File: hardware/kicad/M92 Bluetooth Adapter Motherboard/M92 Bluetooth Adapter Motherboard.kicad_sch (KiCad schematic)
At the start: 26 parts, among them IC1 PIC18F27Q43-I/SO, J2 Conn_Handset_RJ45, J6 Conn_MCU_Programming, J7 Conn_BT_Module, J8 Conn_MCU_IO_UART, Q2 PN2222ATA

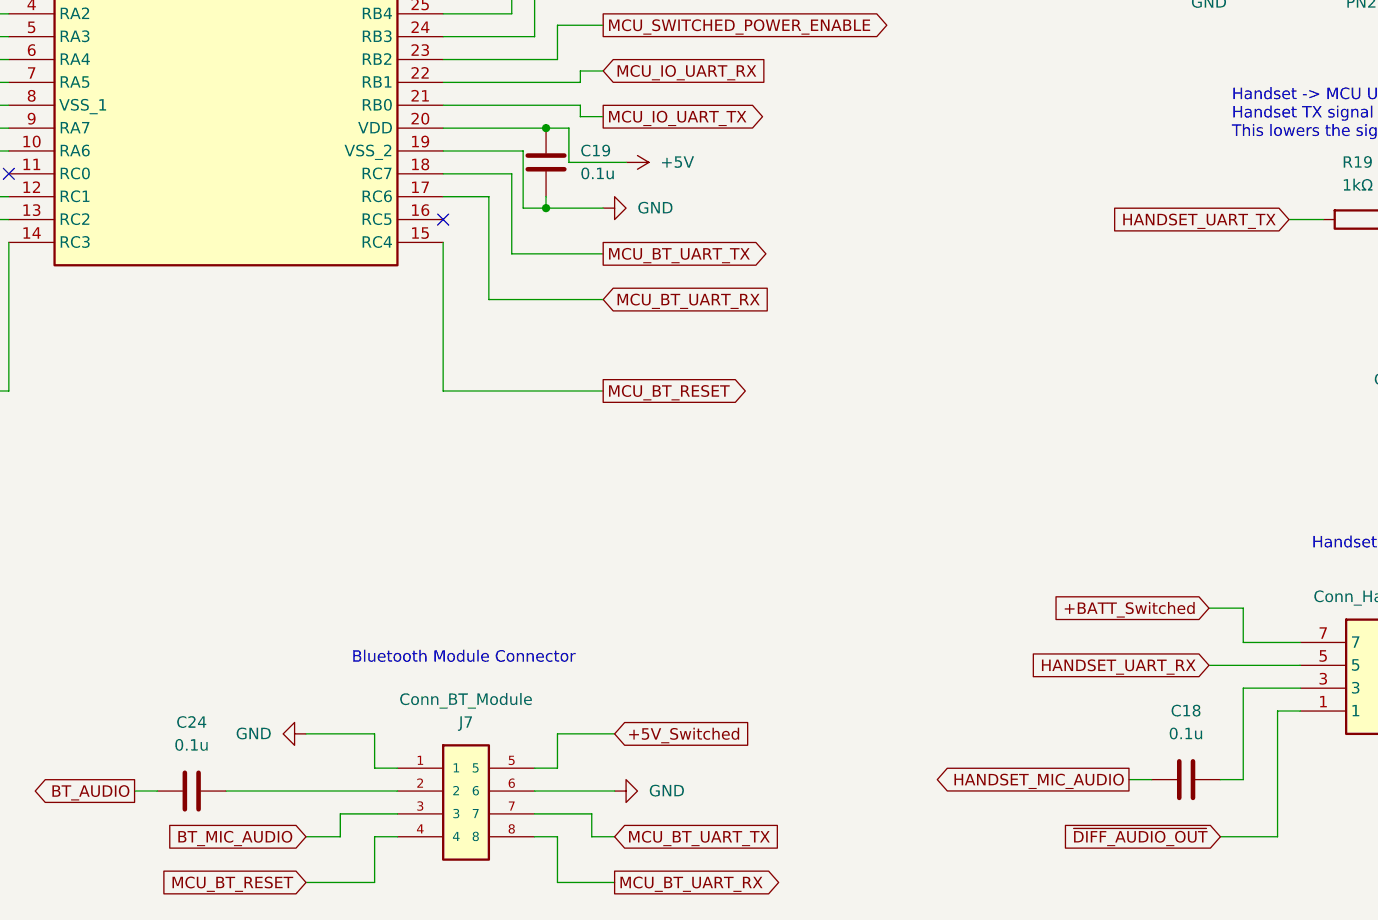
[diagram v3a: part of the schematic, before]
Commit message: Motherboard circuit/PCB adjustments
* Add 100uf cap to stabilize the 5V power supply (reduce voltage dip during power-on of switched 5V supply).
* Add cap to 12V load switch to reduce inrush current when powering on handset.
* Part number updates to more readily available parts.
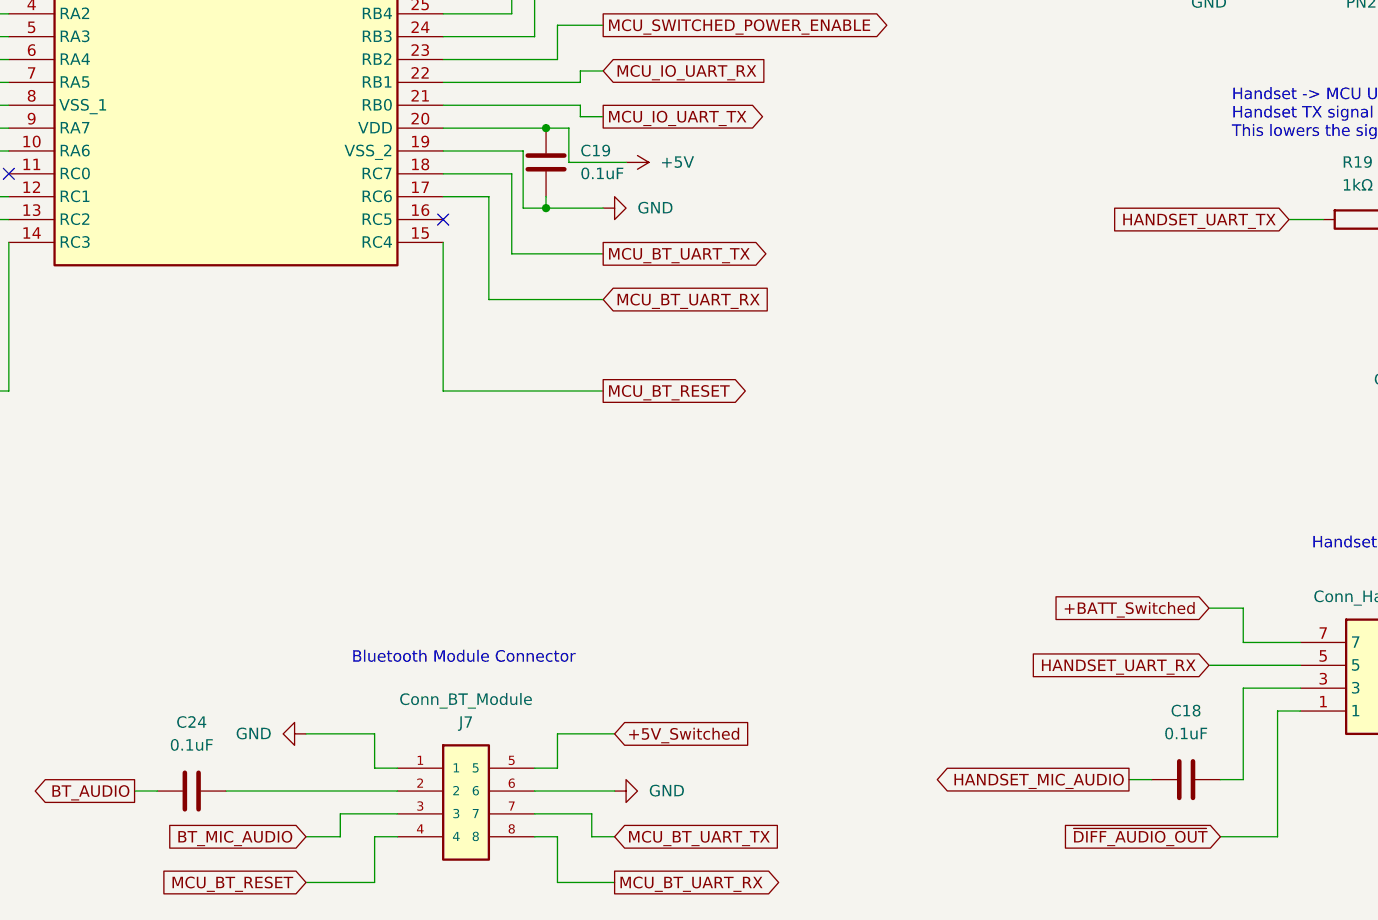
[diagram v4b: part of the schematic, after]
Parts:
- C18, C19, C24: value 0.1u -> 0.1uF
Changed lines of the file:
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@@
       (effects (font (size 1.27 1.27)))
     )
-    (property "Value" "0.1u" (at 96.52 143.51 90)
+    (property "Value" "0.1uF" (at 96.52 143.51 90)
       (effects (font (size 1.27 1.27)))
     )
@@
       (effects (font (size 1.27 1.27)) (justify right))
     )
-    (property "Value" "0.1u" (at 139.7 80.01 0)
+    (property "Value" "0.1uF" (at 139.7 80.01 0)
       (effects (font (size 1.27 1.27)) (justify right))
     )
@@
       (effects (font (size 1.27 1.27)))
     )
-    (property "Value" "0.1u" (at 207.01 142.24 90)
-      (effects (font (size 1.27 1.27)))
-    )
+    (property "Value" "0.1uF" (at 207.01 142.24 90)
+      (effects (font (size 1.27 1.27)))
+    )

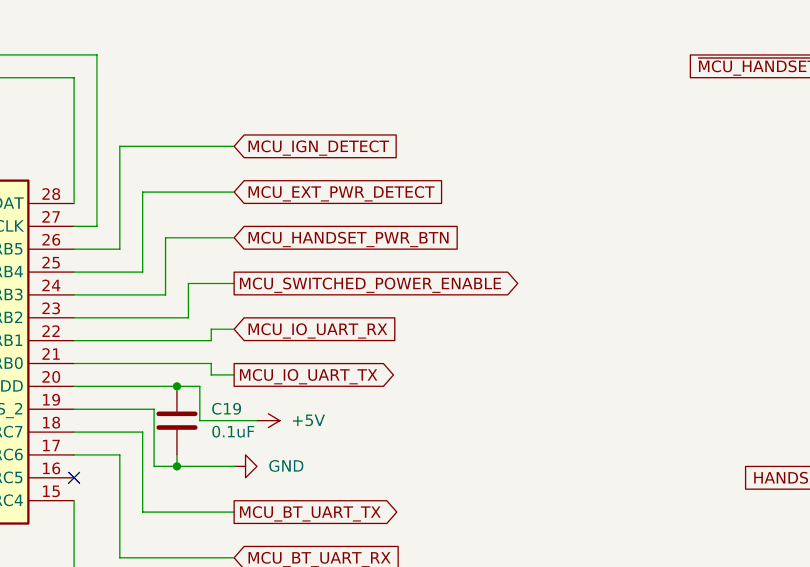
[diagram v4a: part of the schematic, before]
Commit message: Keep handset powered on during restarts
Inverted the switched power enable signal from the MCU with a transistor so that switched power is on by default unless the MCU explicitly disables it. This allows everything to remain powered on while the MCU reboots for a restart. If the MCU is rebooting to power off, then it immediately turns switched power off before entering the sleep state.

This is simpler and more robust than attempting to write code to fully reinitialize ALL MCU state/memory except for switched power enable output.
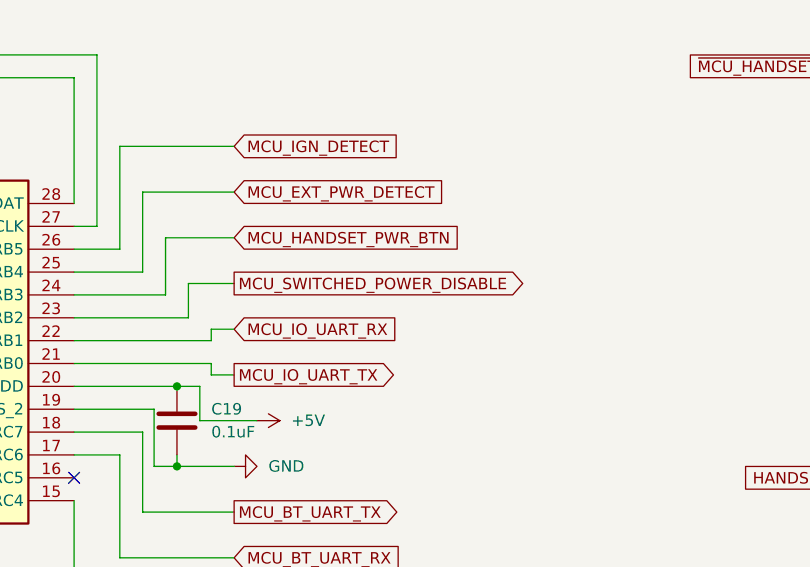
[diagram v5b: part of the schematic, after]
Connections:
- net MCU_SWITCHED_POWER_ENABLE renamed MCU_SWITCHED_POWER_DISABLE
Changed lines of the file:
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@@
     )
   )
-  (global_label "MCU_SWITCHED_POWER_ENABLE" (shape output) (at 142.24 63.5 0) (fields_autoplaced)
+  (global_label "MCU_SWITCHED_POWER_DISABLE" (shape output) (at 142.24 63.5 0) (fields_autoplaced)
     (effects (font (size 1.27 1.27)) (justify left))
-    (property "Intersheetrefs" "${INTERSHEET_REFS}" (at 174.9188 63.5 0)
+    (property "Intersheetrefs" "${INTERSHEET_REFS}" (at 175.5236 63.5 0)
       (effects (font (size 1.27 1.27)) (justify left))
     )

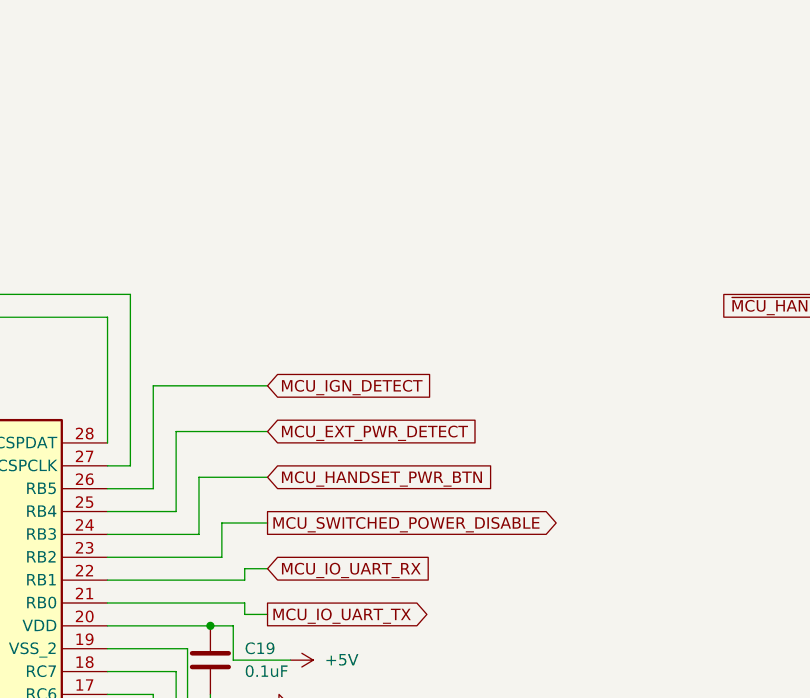
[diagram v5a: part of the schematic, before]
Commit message: Simplify load switch enable circuit, and add 100uF cap to 12V supply
Eliminated the load switch enable inverting transistor and simplified to a combination of a pull-up resistor on the enable pin with open-drain and initially high configuration of the MCU pin.

This still keeps the load switches enabled during a MCU reboot like the previous design, but with fewer components and less wasted power.

Also added a 100uF capacitor to the 12V supply to help reduce voltage dips.
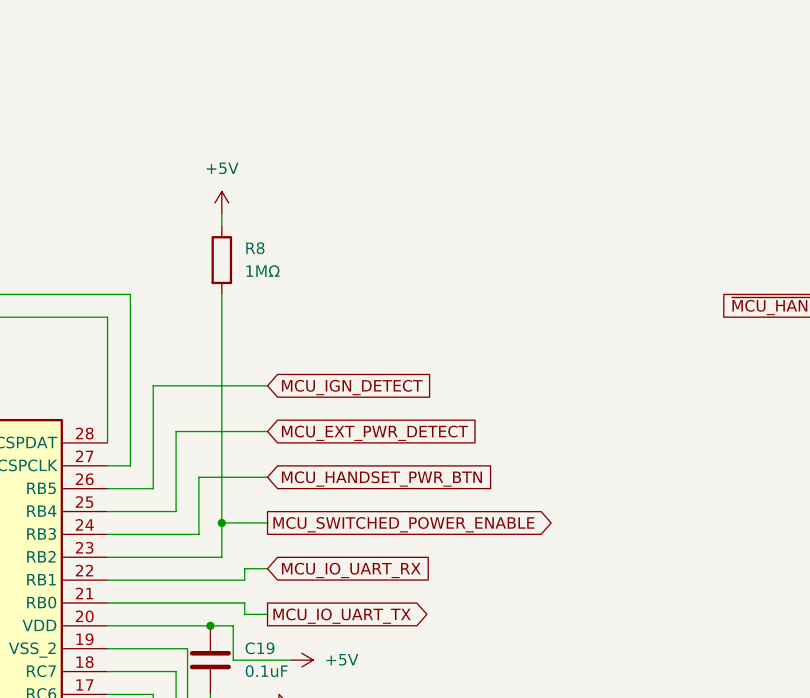
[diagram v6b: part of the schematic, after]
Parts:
- added R8: 1MΩ, Resistor_SMD:R_1206_3216Metric_Pad1.30x1.75mm_HandSolder, symbol Device:R
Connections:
- net +5V: now also R8.1
- net MCU_SWITCHED_POWER_DISABLE renamed MCU_SWITCHED_POWER_ENABLE
- net MCU_SWITCHED_POWER_ENABLE: now also R8.2
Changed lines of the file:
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@@
   (junction (at 135.89 83.82) (diameter 0) (color 0 0 0 0)
+  )
+  (junction (at 137.16 63.5) (diameter 0) (color 0 0 0 0)
   )
   (junction (at 76.2 39.37) (diameter 0) (color 0 0 0 0)
@@
     (stroke (width 0) (type default))
   )
+  (wire (pts (xy 137.16 38.1) (xy 137.16 63.5))
+    (stroke (width 0) (type default))
+  )
   (wire (pts (xy 240.03 53.34) (xy 247.65 53.34))
     (stroke (width 0) (type default))
@@
   )
   (wire (pts (xy 58.42 48.26) (xy 71.12 48.26))
+    (stroke (width 0) (type default))
+  )
+  (wire (pts (xy 137.16 29.21) (xy 137.16 30.48))
     (stroke (width 0) (type default))
   )
@@
     )
   )
-  (global_label "MCU_SWITCHED_POWER_DISABLE" (shape output) (at 142.24 63.5 0) (fields_autoplaced)
-    (effects (font (size 1.27 1.27)) (justify left))
-    (property "Intersheetrefs" "${INTERSHEET_REFS}" (at 175.5236 63.5 0)
+  (global_label "MCU_SWITCHED_POWER_ENABLE" (shape output) (at 142.24 63.5 0) (fields_autoplaced)
+    (effects (font (size 1.27 1.27)) (justify left))
+    (property "Intersheetrefs" "${INTERSHEET_REFS}" (at 174.9188 63.5 0)
       (effects (font (size 1.27 1.27)) (justify left))
     )
@@
     )
   )
+  (symbol (lib_id "power:+5V") (at 137.16 29.21 0) (unit 1)
+    (in_bom yes) (on_board yes) (dnp no) (fields_autoplaced)
+    (property "Reference" "#PWR041" (at 137.16 33.02 0)
+      (effects (font (size 1.27 1.27)) hide)
+    )
+    (property "Value" "+5V" (at 137.16 24.13 0)
+      (effects (font (size 1.27 1.27)))
+    )
+    (property "Footprint" "" (at 137.16 29.21 0)
+      (effects (font (size 1.27 1.27)) hide)
+    )
+    (property "Datasheet" "" (at 137.16 29.21 0)
+      (effects (font (size 1.27 1.27)) hide)
+    )
+    (pin "1")
+    (instances
+      (project "M92 Bluetooth Adapter Motherboard"
+        (path "/d695ac67-4f6c-46c1-9ce6-2d543d3b66ce"
+          (reference "#PWR041") (unit 1)
+        )
+      )
+    )
+  )
   (symbol (lib_id "Mechanical:MountingHole_Pad") (at 53.34 179.07 0) (unit 1)
     (in_bom no) (on_board yes) (dnp no) (fields_autoplaced)
@@
         )
       )
+    )
+  )
+  (symbol (lib_id "Device:R") (at 137.16 34.29 0) (unit 1)
+    (in_bom yes) (on_board yes) (dnp no) (fields_autoplaced)
+    (property "Reference" "R8" (at 139.7 33.02 0)
+      (effects (font (size 1.27 1.27)) (justify left))
+    )
+    (property "Value" "1MΩ" (at 139.7 35.56 0)
+      (effects (font (size 1.27 1.27)) (justify left))
+    )
+    (property "Footprint" "Resistor_SMD:R_1206_3216Metric_Pad1.30x1.75mm_HandSolder" (at 135.382 34.29 90)
+      (effects (font (size 1.27 1.27)) hide)
+    )
+    (property "Datasheet" "https://www.mouser.com/datasheet/2/54/cr-1858361.pdf" (at 137.16 34.29 0)
+      (effects (font (size 1.27 1.27)) hide)
+    )
+    (property "Height" "0.6" (at 137.16 34.29 0)
+      (effects (font (size 1.27 1.27)) hide)
+    )
+    (property "Manufacturer_Name" "Bourns" (at 137.16 34.29 0)
+      (effects (font (size 1.27 1.27)) hide)
+    )
+    (property "Manufacturer_Part_Number" "CR1206-FX-1004ELF" (at 137.16 34.29 0)
+      (effects (font (size 1.27 1.27)) hide)
+    )
+    (property "Mouser Part Number" "652-CR1206FX-1004ELF" (at 137.16 34.29 0)
+      (effects (font (size 1.27 1.27)) hide)
+    )
+    (property "Mouser Price/Stock" "https://www.mouser.com/ProductDetail/Bourns/CR1206-FX-1004ELF?qs=sGAEpiMZZMvdGkrng054t%2Fh5BnJxeWSzTqpm%252BH9NqIU%3D" (at 137.16 34.29 0)
+      (effects (font (size 1.27 1.27)) hide)
+    )
+    (property "JLCPCB Part #" "C17927" (at 137.16 34.29 0)
+      (effects (font (size 1.27 1.27)) hide)
+    )
+    (pin "1")
+    (pin "2")
+    (instances
+      (project "M92 Bluetooth Adapter Motherboard"
+        (path "/d695ac67-4f6c-46c1-9ce6-2d543d3b66ce/8852b3cd-e5e9-4a63-b614-38055f92a00c"
+          (reference "R8") (unit 1)
+        )
+        (path "/d695ac67-4f6c-46c1-9ce6-2d543d3b66ce"
+          (reference "R8") (unit 1)
+        )
+      )

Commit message: Minor schematic/pcb fixes
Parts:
- J2: Manufacturer_Part_Number GLX-N-88M-BLK -> GLX-N-88M; Mouser Part Number 806-GLX-N-88M-BLK -> 806-GLX-N-88M; Mouser Price/Stock https://www.mouser.com/ProductDetail/Kycon/GLX-N-88M-BLK?qs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 -> https://www.mouser.com/ProductDetail/Kycon/GLX-N-88M?qs=1jN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
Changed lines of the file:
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@@
       (effects (font (size 1.27 1.27)) (justify left top) hide)
     )
-    (property "Mouser Part Number" "806-GLX-N-88M-BLK" (at 236.22 627 0)
+    (property "Mouser Part Number" "806-GLX-N-88M" (at 236.22 627 0)
       (effects (font (size 1.27 1.27)) (justify left top) hide)
     )
-    (property "Mouser Price/Stock" "https://www.mouser.com/ProductDetail/Kycon/GLX-N-88M-BLK?qs=moKBCcMDJAVKDCLBxfYIfw%3D%3D" (at 236.22 727 0)
+    (property "Mouser Price/Stock" "https://www.mouser.com/ProductDetail/Kycon/GLX-N-88M?qs=1jNLoGjawi%252BjOyV6m6lU7w%3D%3D" (at 236.22 727 0)
       (effects (font (size 1.27 1.27)) (justify left top) hide)
     )
@@
       (effects (font (size 1.27 1.27)) (justify left top) hide)
     )
-    (property "Manufacturer_Part_Number" "GLX-N-88M-BLK" (at 236.22 927 0)
+    (property "Manufacturer_Part_Number" "GLX-N-88M" (at 236.22 927 0)
       (effects (font (size 1.27 1.27)) (justify left top) hide)
     )
